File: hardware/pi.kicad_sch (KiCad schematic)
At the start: 10 parts, among them J1 OPI_Z3_26PIN, J10 AUX 5V (screen), J2 OPI_BREAKOUT, J3 UART5 ttyAS5, J4 UART2 ttyAS2, J8 I2C3 spare, J9 FAN 5V

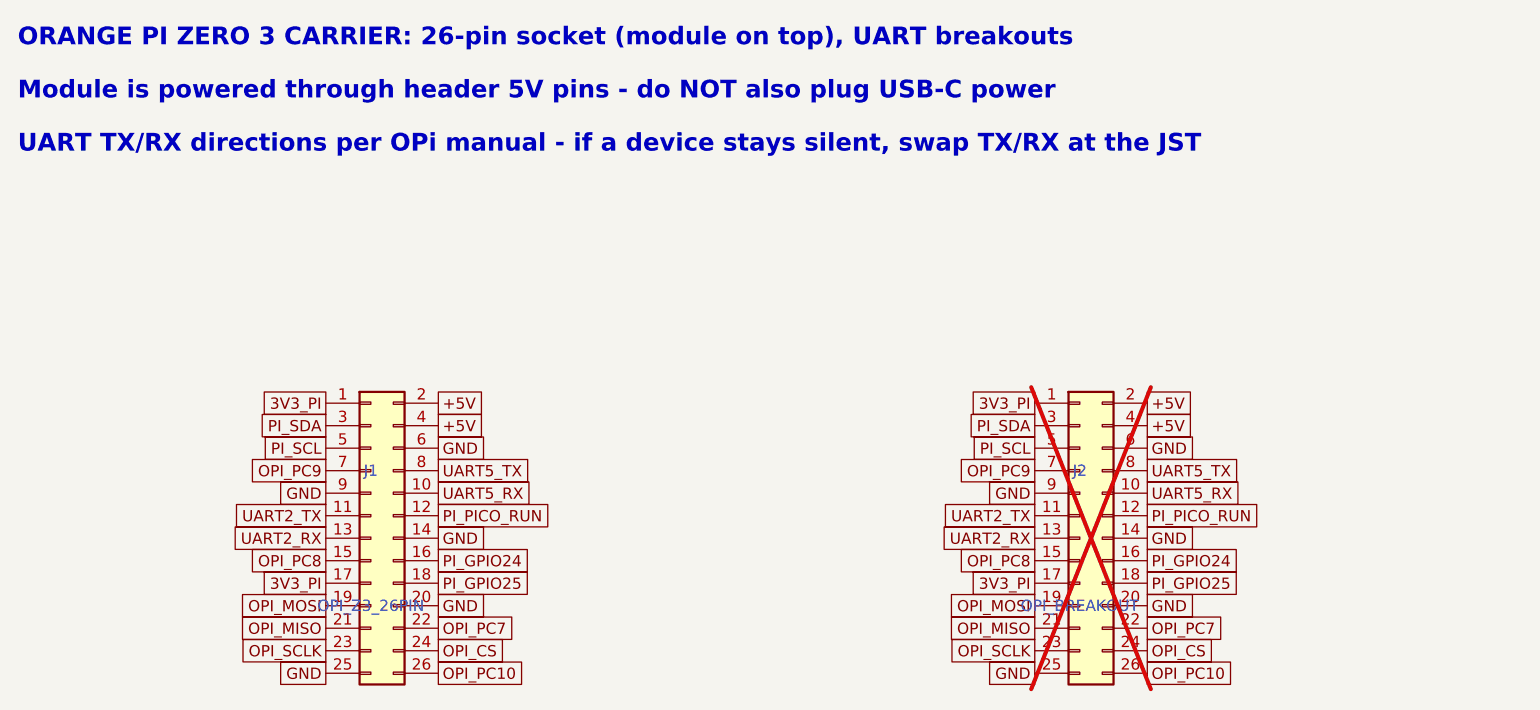
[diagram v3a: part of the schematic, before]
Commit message: feat: v4.1 — J1 male header for 26-way IDC ribbon (pre-soldered Zero 3), J1.14/J2.9 NC by design, clearance 0.14; DRC clean
Co-Authored-By: Claude Fable 5 <noreply@anthropic.com>
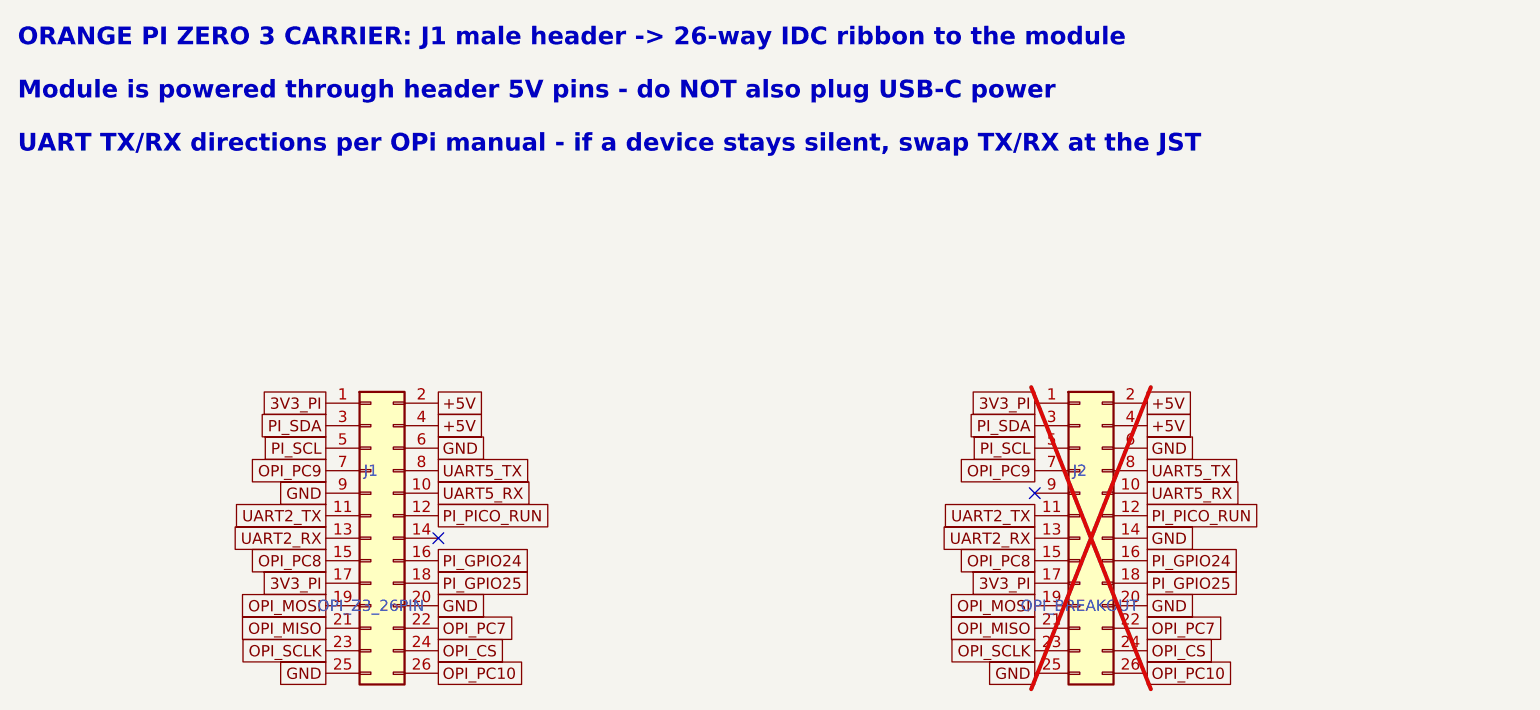
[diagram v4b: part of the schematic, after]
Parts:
- J1: footprint Connector_PinSocket_2.54mm:PinSocket_2x13_P2.54mm_Vertical -> Connector_PinHeader_2.54mm:PinHeader_2x13_P2.54mm_Vertical
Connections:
- net GND: no longer J1.14 (Pin_14), J2.9 (Pin_9)
- no-connect marks 0 -> 2
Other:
- note added: "ORANGE PI ZERO 3 CARRIER: J1 male header -> 26-way IDC ribbon to the module"
- note removed: "ORANGE PI ZERO 3 CARRIER: 26-pin socket (module on top), UART breakouts"
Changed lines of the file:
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@@
   (generator_version "8.0")
   (paper "A3")
-  (text "ORANGE PI ZERO 3 CARRIER: 26-pin socket (module on top), UART breakouts" (exclude_from_sim no) (at 30 40 0)
+  (text "ORANGE PI ZERO 3 CARRIER: J1 male header -> 26-way IDC ribbon to the module" (exclude_from_sim no) (at 30 40 0)
     (effects (font (size 2 2) (bold yes)) (justify left bottom))
   )
@@
     (property "Value" "OPI_Z3_26PIN" (at 69.85 102.87 0)
       (effects (font (size 1.27 1.27))))
-    (property "Footprint" "Connector_PinSocket_2.54mm:PinSocket_2x13_P2.54mm_Vertical" (at 69.85 95.25 0)
+    (property "Footprint" "Connector_PinHeader_2.54mm:PinHeader_2x13_P2.54mm_Vertical" (at 69.85 95.25 0)
       (effects (font (size 1.27 1.27)) (hide yes)))
     (property "Datasheet" "" (at 69.85 95.25 0)
@@
       (effects (font (size 1.27 1.27)) (hide yes)))
   )
-  (global_label "GND" (shape passive) (at 77.47 95.25 0.0) (fields_autoplaced yes)
-    (effects (font (size 1.27 1.27)) (justify left))
-    (property "Intersheetrefs" "${INTERSHEET_REFS}" (at 77.47 95.25 0)
-      (effects (font (size 1.27 1.27)) (hide yes)))
-  )
   (global_label "OPI_PC8" (shape passive) (at 64.77 97.79 180.0) (fields_autoplaced yes)
     (effects (font (size 1.27 1.27)) (justify right))
@@
       (effects (font (size 1.27 1.27)) (hide yes)))
   )
-  (global_label "GND" (shape passive) (at 144.78 90.17 180.0) (fields_autoplaced yes)
-    (effects (font (size 1.27 1.27)) (justify right))
-    (property "Intersheetrefs" "${INTERSHEET_REFS}" (at 144.78 90.17 0)
-      (effects (font (size 1.27 1.27)) (hide yes)))
-  )
   (global_label "UART5_RX" (shape passive) (at 157.48 90.17 0.0) (fields_autoplaced yes)
     (effects (font (size 1.27 1.27)) (justify left))
@@
       (effects (font (size 1.27 1.27)) (hide yes)))
   )
+  (no_connect (at 77.47 95.25))
+  (no_connect (at 144.78 90.17))
 )
